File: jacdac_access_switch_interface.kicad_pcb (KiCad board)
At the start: 2 copper layers, 35 x 35 mm, 42 parts, among them J1 Conn_Jacdac_CardEdge, J2 Conn_HackConnect, J3 pj313d, J4 jack_3.5_pj313d, SW1 SW_PTS810, U1 NCP114ASN330T1G, U2 STM32G030F6P6, U3 TLP240A, U4 TLP240A

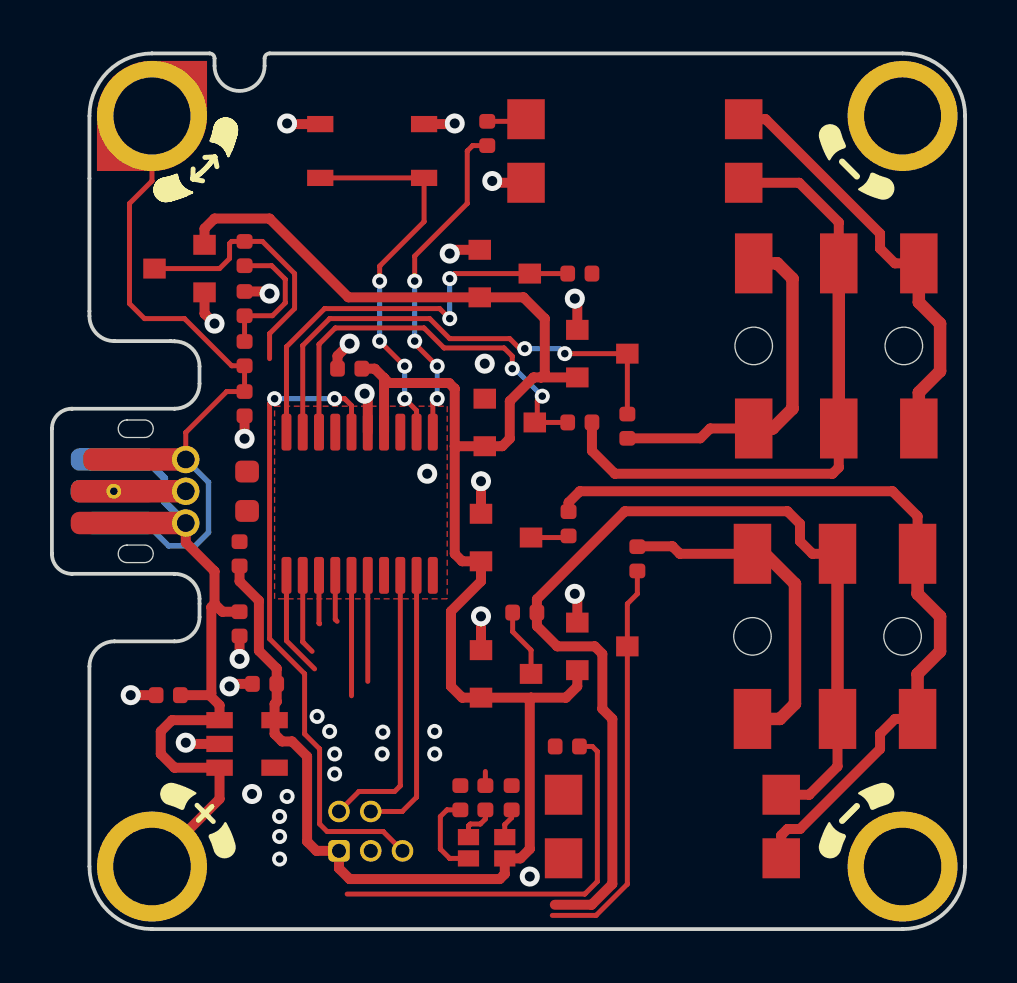
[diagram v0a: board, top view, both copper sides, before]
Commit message: Reassigned pins on MCU and spun MCU, routing ongoing
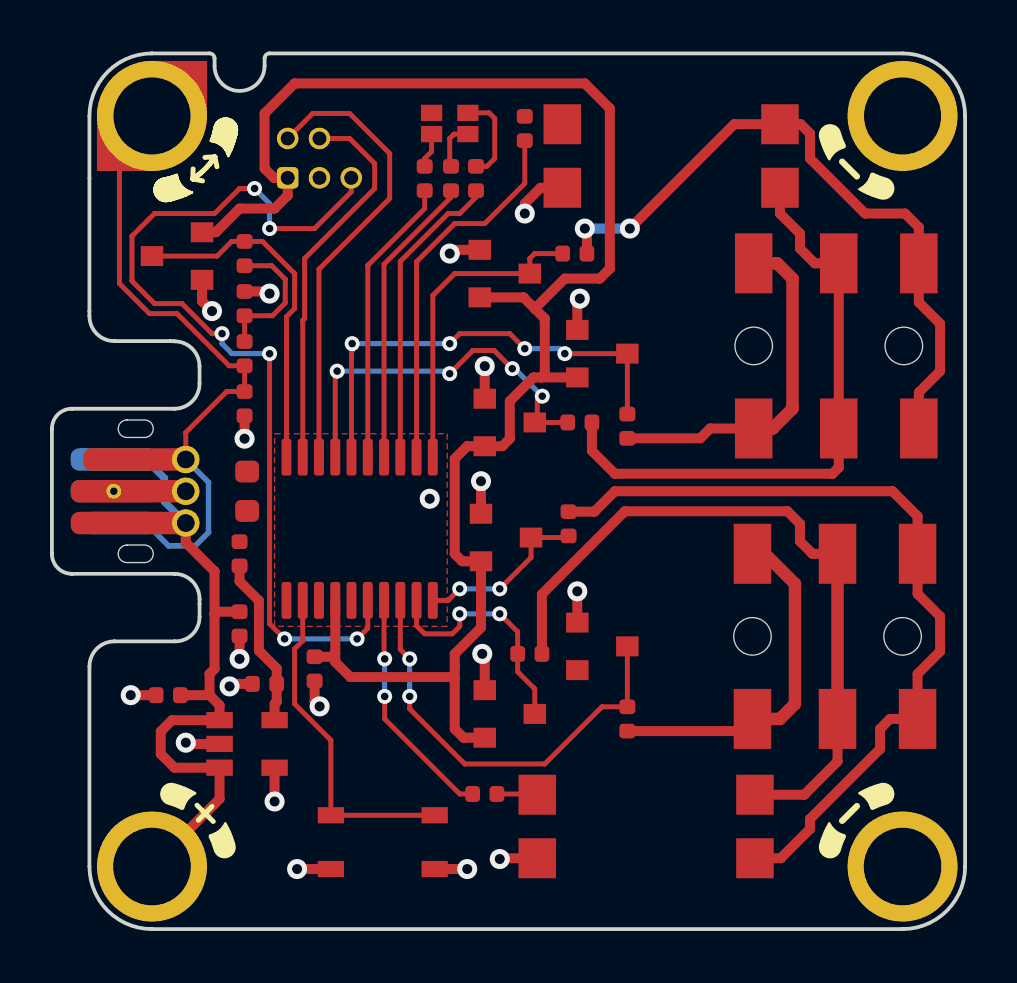
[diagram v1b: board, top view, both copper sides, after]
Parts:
- moved D5 29.0 mm to (161.9, 70.3), turned to -90 degrees
- moved SW1 27.6 mm to (159.2, 99.0), turned to 180 degrees
- moved J2 27.0 mm to (156.7, 71.7)
- moved R8 25.0 mm to (160.9, 72.5), turned to -90 degrees
- moved R7 24.8 mm to (161.9, 72.5), turned to -90 degrees
- moved R6 24.8 mm to (162.9, 72.5), turned to -90 degrees
- moved C4 12.1 mm to (156.5, 92.1), turned to -90 degrees
- moved R11 6.41 mm to (169.0, 94.1), turned to 90 degrees
- moved R2 3.81 mm to (163.3, 97.1), turned to 180 degrees
- moved R12 1.66 mm to (165.1, 91.5)
- moved D10 1.61 mm to (164.3, 93.9)
- moved R3 1.51 mm to (164.9, 70.5)
- moved U4 1.46 mm to (170.7, 71.7)
- moved U3 1.05 mm to (169.7, 98.5)
- moved U2 1.00 mm to (158.3, 86.5), turned to 90 degrees
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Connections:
- U2 pad 1: /RELAY1 -> unconnected-(U2-PB7/PB8)
- U2 pad 10: /SLEEVE1_P -> /SLEEVE2_P
- U2 pad 11: /RELAY2 -> /SLEEVE1_P
- U2 pad 12: /SLEEVE2_P -> /RELAY1
- U2 pad 13: /RING2_P -> /RGB_R
- U2 pad 14: /TIP2_P -> /RGB_G
- U2 pad 15: /RGB_R -> /RGB_B
- U2 pad 16: /RGB_G -> /RING1_P
- U2 pad 17: unconnected-(U2-PA12[PA10]) -> /TIP1_P
- U2 pad 7: unconnected-(U2-PA0) -> /RELAY2
- U2 pad 8: /TIP1_P -> /RING2_P
- U2 pad 9: /RING1_P -> /TIP2_P
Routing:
- net /TIP2: track 42.0 -> 28.8 mm
- net /RGB_B: track 0.00 -> 11.6 mm
- net /RELAY2: track 20.4 -> 9.51 mm
- net /nRESET: track 25.9 -> 36.8 mm, vias 2 -> 6
- net /SLEEVE1: track 17.0 -> 27.2 mm, vias 0 -> 2
- net /RGB_R: track 4.81 -> 12.2 mm, vias 2 -> 0
- net /SWDIO: track 11.5 -> 18.5 mm
- net /RGB_G: track 4.84 -> 11.8 mm, vias 2 -> 0
- net +3V3: track 80.3 -> 73.9 mm
- net /TIP2_P: track 4.62 -> 9.68 mm
- net /SWDCLK: track 10.9 -> 15.5 mm
- net /SLEEVE1_P: track 17.1 -> 12.7 mm, vias 2 -> 0
- net GND: track 20.8 -> 24.3 mm, vias 21 -> 20
- net /JD_DATA_MCU: track 10.7 -> 13.9 mm
- net /nFLASH: track 15.9 -> 13.5 mm, vias 4 -> 0
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
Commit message: Routing for PCB v1.7 complete
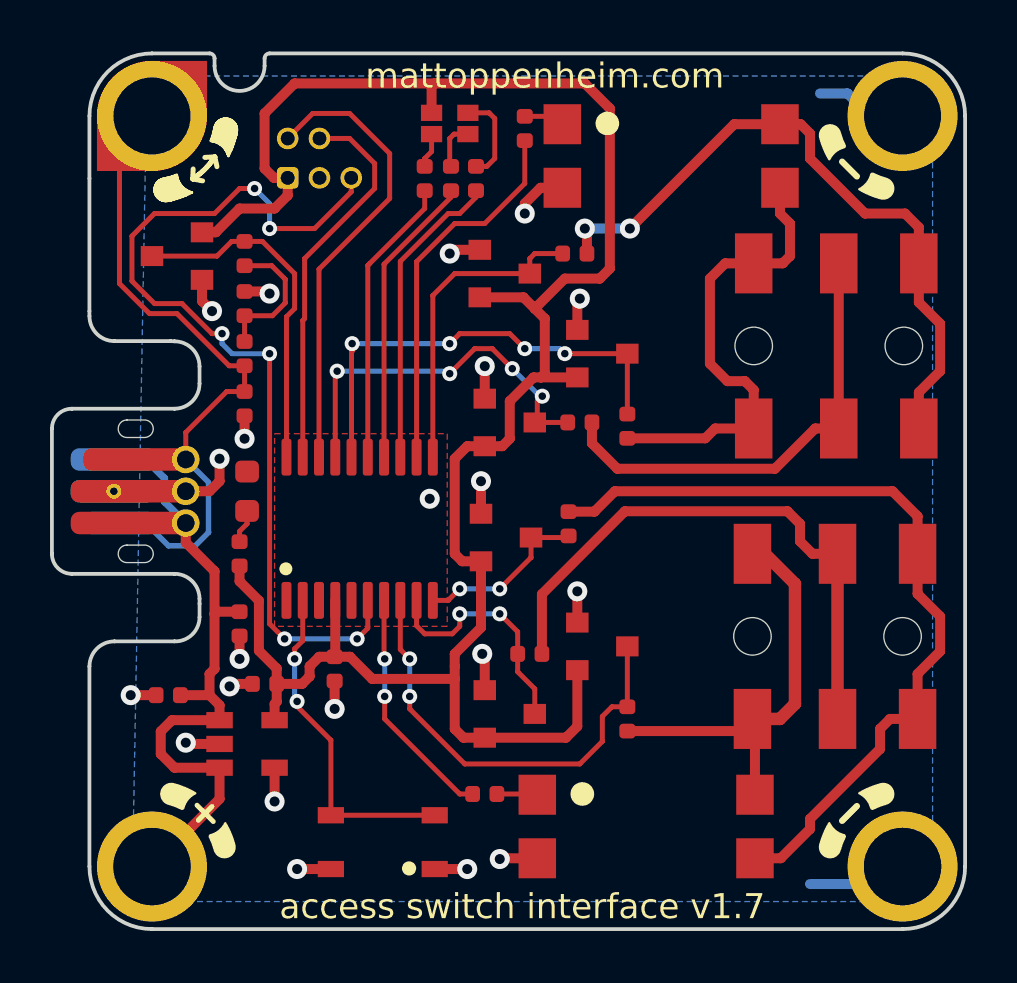
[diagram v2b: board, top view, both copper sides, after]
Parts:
- moved C4 0.80 mm to (157.3, 92.1)
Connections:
- D10 pad 3: /TIP2_P -> /RING2_P
- D6 pad 3: /RING1_P -> /TIP1_P
- D7 pad 3: /TIP1_P -> /RING1_P
- D9 pad 3: /RING2_P -> /TIP2_P
- R11 pad 1: /RING2 -> /TIP2
- R11 pad 2: /RING2_P -> /TIP2_P
- R12 pad 1: /TIP2 -> /RING2
- R12 pad 2: /TIP2_P -> /RING2_P
- R5 pad 1: /RING1 -> /TIP1
- R5 pad 2: /RING1_P -> /TIP1_P
- R9 pad 1: /TIP1 -> /RING1
- R9 pad 2: /TIP1_P -> /RING1_P
- U2 pad 16: /RING1_P -> /TIP1_P
- U2 pad 17: /TIP1_P -> /RING1_P
- U2 pad 8: /RING2_P -> /TIP2_P
- U2 pad 9: /TIP2_P -> /RING2_P
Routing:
- net /TIP2: track 28.8 -> 17.2 mm
- net GND: track 24.3 -> 34.4 mm, vias 20 -> 21
- net +3V3: track 73.9 -> 83.2 mm
- net /RING2: track 14.1 -> 23.3 mm
- net /TIP2_P: track 9.68 -> 18.1 mm
- net /RING2_P: track 17.5 -> 9.68 mm
- net /TIP1: track 24.2 -> 18.8 mm
- net /RING1: track 13.9 -> 18.4 mm
- net /RING1_P: track 18.5 -> 15.4 mm
- net /TIP1_P: track 15.4 -> 18.5 mm
- net Net-(R3-Pad1): track 0.00 -> 1.63 mm
- net Net-(D12-A): track 0.00 -> 1.35 mm
- net /nFLASH: vias 0 -> 2
- added copper zone on B.Cu, net GND
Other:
- board text added: "access switch interface v1.7"
- board text added: "mattoppenheim.com"
- board text removed: "Access switch interface v1.7 mattoppenheim.com"

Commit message: v1.7 complete and sent for manufacture
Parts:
- added G***: LOGO, jacdac_access_switch_interface:qr_code_20mm, B.Cu at (163.0, 84.9)
- J3: value pj313d -> jack_3.5_pj313d
- moved C2 0.90 mm to (153.6, 92.7)
- moved C1 0.51 mm to (150.4, 93.6)
- moved U2 0.30 mm to (158.6, 86.5)
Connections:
- U2 pad 1: unconnected-(U2-PB7/PB8) -> /JD_STATUS
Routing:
- net /JD_STATUS: track 0.00 -> 10.0 mm, vias 0 -> 2
- net GND: track 34.4 -> 41.9 mm
- net /nRESET: track 36.8 -> 39.3 mm
- net +3V3: track 83.2 -> 84.6 mm
- net JD_PWR: track 21.9 -> 20.8 mm
- net /RING2_P: track 9.68 -> 8.75 mm
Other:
- rule pad_to_mask_clearance: 0.05 -> 0
- board text added: "1"
- board text added: "2"
